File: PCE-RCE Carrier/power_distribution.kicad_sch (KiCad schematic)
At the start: 31 parts, among them J2 XT60PW-F, J3 XT30UPB-M, J4 XT60PW-F, J8 Conn_01x02_Pin, J9 XT30UPB-M, U1 TPS75533KTTRG3, U2 TPS54302DDCR, U3 BD6222HFP-TR, U4 LMR51430, U5 BD6222HFP-TR

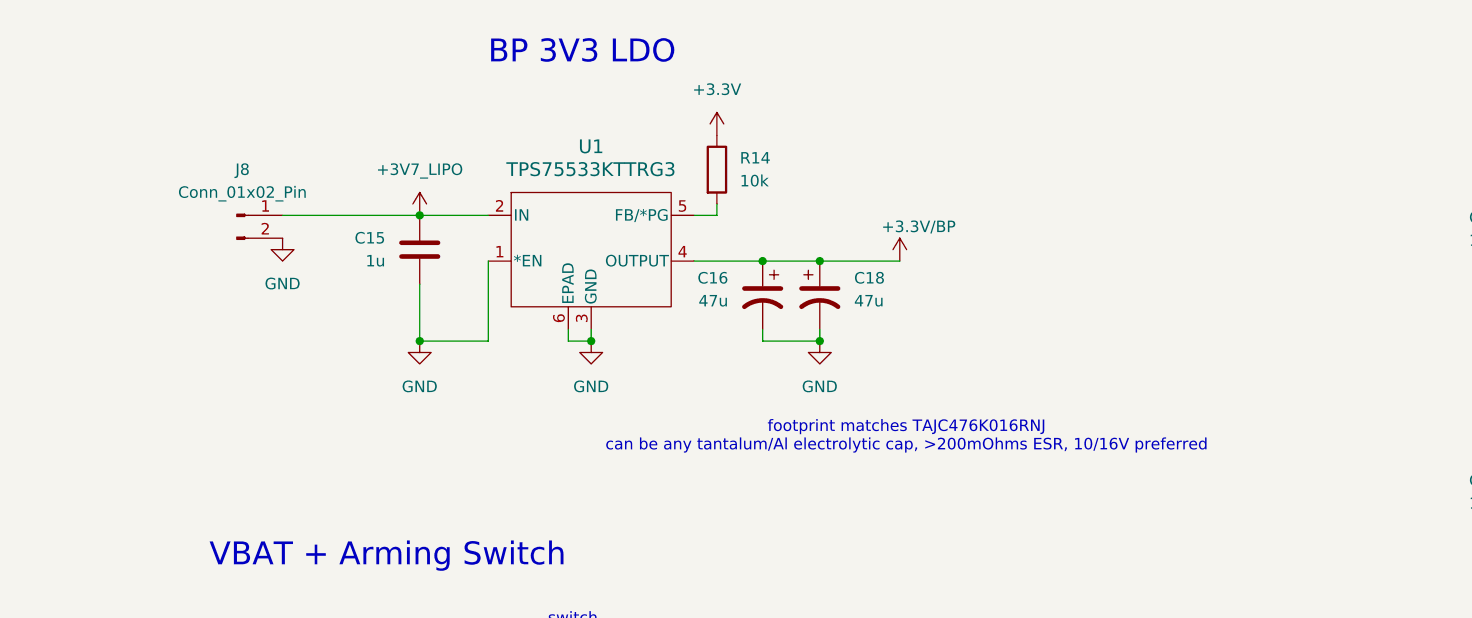
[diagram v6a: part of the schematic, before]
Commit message: split pce and rce functions into two carriers, initial rce parts placement
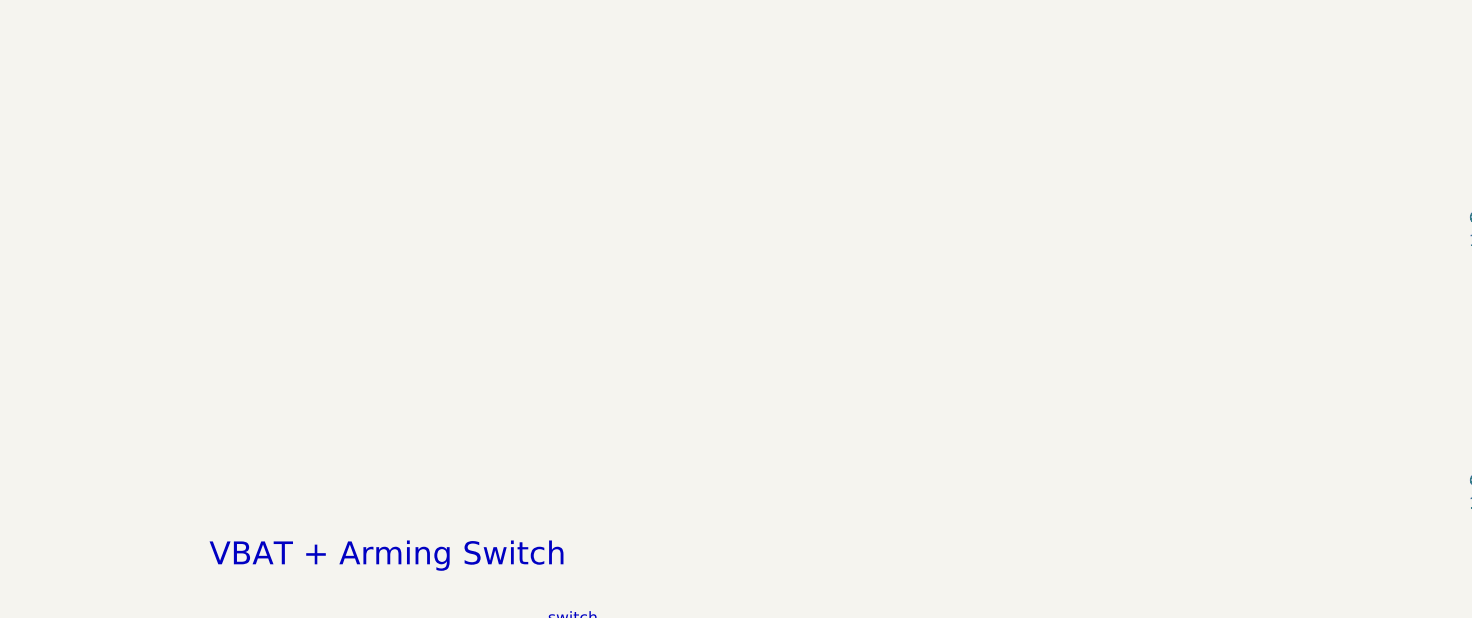
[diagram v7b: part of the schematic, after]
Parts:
- removed C15: 1u, Capacitor_SMD:C_0805_2012Metric, symbol Device:C
- removed C16, C18: 47u, Capacitor_Tantalum_SMD:CP_EIA-6032-28_Kemet-C, symbol Device:C_Polarized_US
- removed J8: Conn_01x02_Pin, Connector_JST:JST_PH_B2B-PH-K_1x02_P2.00mm_Vertical, symbol Connector:Conn_01x02_Pin
- removed R14: 10k, Resistor_SMD:R_0402_1005Metric, symbol Device:R
- removed U1: TPS75533KTTRG3, KTT5_6P22X6P86, symbol TPS75533KTRRG3:TPS75533KTTRG3
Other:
- note removed: "BP 3V3 LDO"
- note removed: "footprint matches TAJC476K016RNJ can be any tantalum/Al electrolytic cap, >200mOhms ESR, 10/16V preferred"
- title: PCE & RCE Power Distribution and Motor Control -> PCE Power Distribution and Motor Control

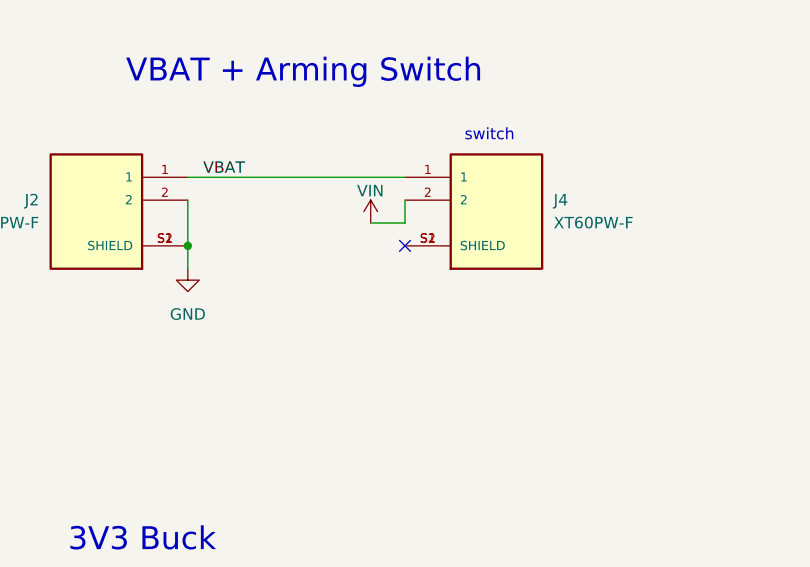
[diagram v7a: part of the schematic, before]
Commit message: PCE wiring except solenoids and 3V3 in
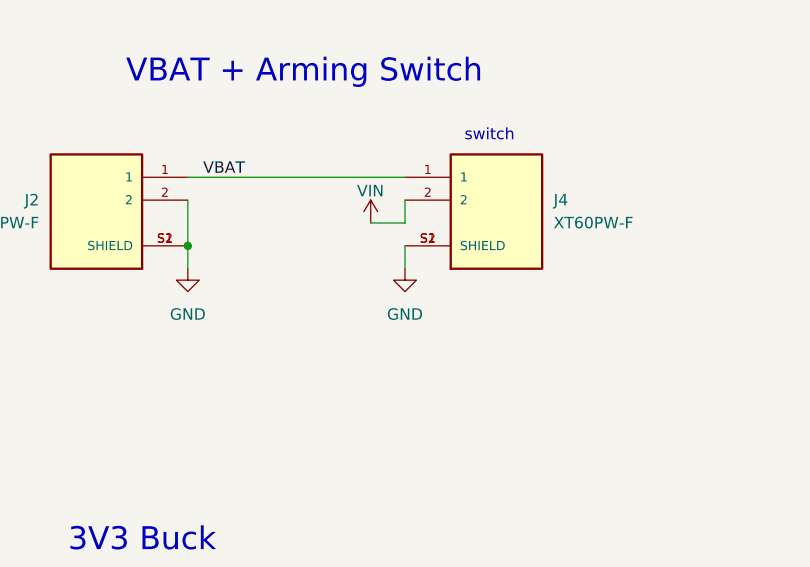
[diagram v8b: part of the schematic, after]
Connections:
- net GND: now also J4.S1 (SHIELD), J4.S2 (SHIELD)
- no-connect marks 1 -> 0
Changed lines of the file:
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@@
 		(color 0 0 0 0)
 	)
-	(no_connect
-		(at 87.63 93.98)
-	)
 	(wire
 		(pts
@@
 		(pts
 			(xy 40.64 139.7) (xy 30.48 139.7)
+		)
+		(stroke
+			(width 0)
+			(type default)
+		)
+	)
+	(wire
+		(pts
+			(xy 87.63 93.98) (xy 87.63 96.52)
 		)
 		(stroke
@@
 					(unit 1)
 				)
+			)
+		)
+	)
+	(symbol
+		(lib_id "power:GND")
+		(at 87.63 96.52 0)
+		(mirror y)
+		(unit 1)
+		(body_style 1)
+		(exclude_from_sim no)
+		(in_bom yes)
+		(on_board yes)
+		(in_pos_files yes)
+		(dnp no)
+		(fields_autoplaced yes)
+		(property "Reference" "#PWR020"
+			(at 87.63 102.87 0)
+			(hide yes)
+			(show_name no)
+			(do_not_autoplace no)
+			(effects
+				(font
+					(size 1.27 1.27)
+				)
+			)
+		)
+		(property "Value" "GND"
+			(at 87.63 101.6 0)
+			(show_name no)
+			(do_not_autoplace no)
+			(effects
+				(font
+					(size 1.27 1.27)
+				)
+			)
+		)
+		(property "Footprint" ""
+			(at 87.63 96.52 0)
+			(hide yes)
+			(show_name no)
+			(do_not_autoplace no)
+			(effects
+				(font
+					(size 1.27 1.27)
+				)
+			)
+		)
+		(property "Datasheet" ""
+			(at 87.63 96.52 0)
+			(hide yes)
+			(show_name no)
+			(do_not_autoplace no)
+			(effects
+				(font
+					(size 1.27 1.27)
+				)
+			)
+		)
+		(property "Description" "Power symbol creates a global label with name \"GND\" , ground"
+			(at 87.63 96.52 0)
+			(hide yes)
+			(show_name no)
+			(do_not_autoplace no)
+			(effects
+				(font
+					(size 1.27 1.27)
+				)
+			)
+		)
+		(pin "1"
+		)
+		(instances
+			(project "PCE-RCE Carrier"
+				(path "/061bd5f9-7321-49d7-bd52-d55a9dc51a00/b13c5c10-72c7-47f9-aac2-179cc68eb567"
+					(reference "#PWR020")
+					(unit 1)
+				)
